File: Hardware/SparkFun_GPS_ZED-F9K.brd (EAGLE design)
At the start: 43.2 x 50.8 mm, 148 parts, among them J3 QWIIC_RIGHT_ANGLE, J4 QWIIC_RIGHT_ANGLE, U1 DUAL-OPTO_HCPL-073L, U2 U-BLOX_ZED_F9R, U3 UHS_INVERTER_SCHMITT_TRIGGERS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, U4 UHS_INVERTER_SCHMITT_TRIGGERS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, U5 3.3V

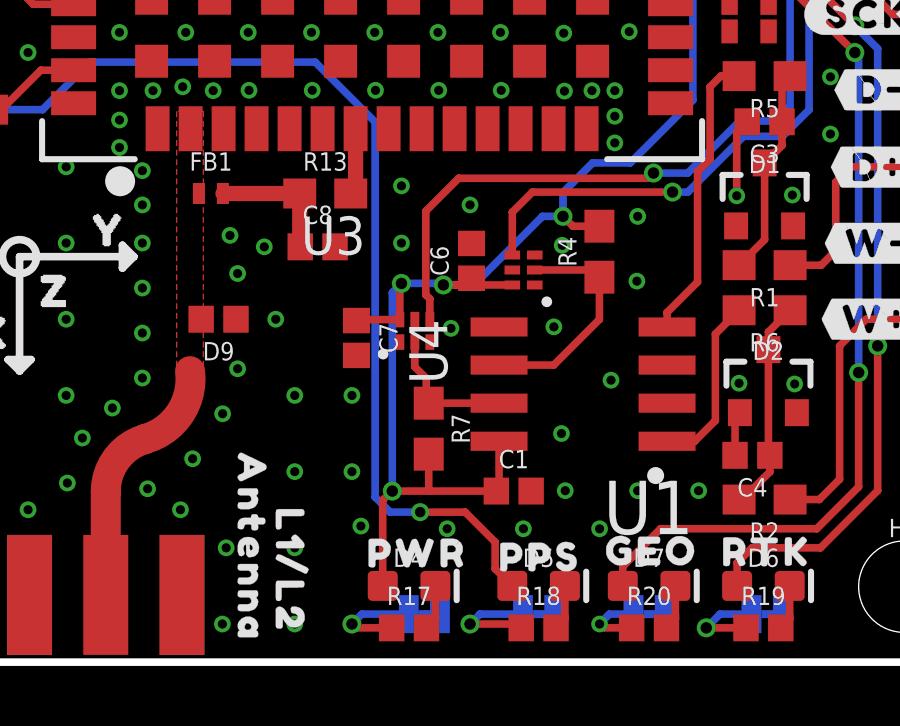
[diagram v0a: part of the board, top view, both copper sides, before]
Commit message: Updates libraries, replaces F9R with F9K, fixes some text in schematic, deletes blank sheets in schematic
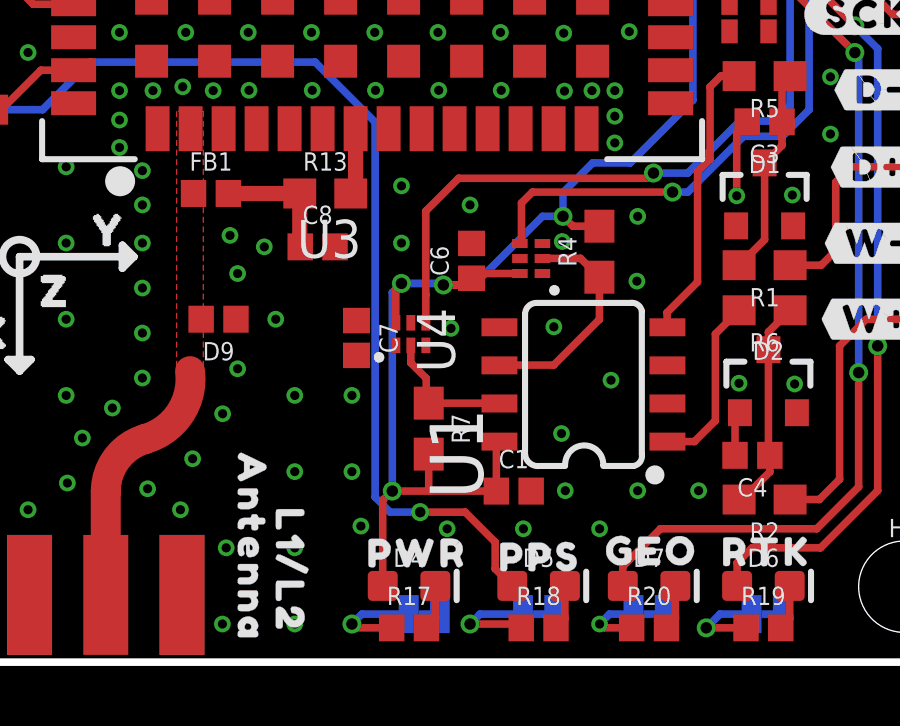
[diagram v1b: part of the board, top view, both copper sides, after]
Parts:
- FB1: value 120NH -> 120Ω; device SparkFun-Coils:0402_MURATA -> SparkFun-Coils:0402
- U1: value DUAL-OPTO_HCPL-073L -> DUAL-OPTO_HCPL-073LSOIC-8; device SparkFun-DiscreteSemi:SOP_8-PIN -> SparkFun-DiscreteSemi:SO08
- U2: value U-BLOX_ZED_F9R -> U-BLOX_ZED_F9K; device SparkFun-GPS:UBLOX_ZED_F9R -> f9k:UBLOX_ZED_F9K
- moved U4 0.46 mm to (28.2, 13.5)
- moved U1 0.19 mm to (29.9, 9.26), turned to 90 degrees
- moved U3 0.17 mm to (24.2, 10.9)
- renumbered JP1 to PWR, JP2 to PPS, JP3 to RTK, JP4 to GEO, JP5 to SPI
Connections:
- net 3.3V: now also U1.8; no longer U1.P8
- net DIR_IN: now also U1.4; no longer U1.P4
- net DIR_SCHMITT: now also U1.6; no longer U1.P6
- net GND: now also U1.2, U1.3, U1.5; no longer U1.P2, U1.P3, U1.P5
- net N$5: now also FB1.2; no longer FB1.P2
- net RF_IN: now also FB1.1; no longer FB1.P1
- net WT_IN: now also U1.1; no longer U1.P1
- net WT_SCHMITT: now also U1.7; no longer U1.P7
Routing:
- net 3.3V: track 133.9 -> 133.4 mm

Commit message: Updates script being used
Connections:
- net DIR_SCHMITT renamed DIR_INV
- net WT_SCHMITT renamed WT_INV
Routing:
- net 3.3V: track 133.4 -> 134.7 mm
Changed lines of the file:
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@@
 <setting verticaltext="up"/>
 </settings>
-<grid distance="0.05" unitdist="inch" unit="inch" style="lines" multiple="1" display="yes" altdistance="0.005" altunitdist="inch" altunit="inch"/>
+<grid distance="0.05" unitdist="inch" unit="inch" style="dots" multiple="1" display="yes" altdistance="0.005" altunitdist="inch" altunit="inch"/>
 <layers>
 <layer number="1" name="Top" color="4" fill="1" visible="yes" active="yes"/>
@@
 <layer number="19" name="Unrouted" color="6" fill="1" visible="yes" active="yes"/>
 <layer number="20" name="Dimension" color="15" fill="1" visible="yes" active="yes"/>
-<layer number="21" name="tPlace" color="16" fill="1" visible="no" active="yes"/>
-<layer number="22" name="bPlace" color="14" fill="1" visible="no" active="yes"/>
+<layer number="21" name="tPlace" color="16" fill="1" visible="yes" active="yes"/>
+<layer number="22" name="bPlace" color="14" fill="1" visible="yes" active="yes"/>
 <layer number="23" name="tOrigins" color="15" fill="1" visible="yes" active="yes"/>
 <layer number="24" name="bOrigins" color="15" fill="1" visible="yes" active="yes"/>
@@
 <layer number="37" name="tTest" color="7" fill="1" visible="no" active="yes"/>
 <layer number="38" name="bTest" color="7" fill="1" visible="no" active="yes"/>
-<layer number="39" name="tKeepout" color="4" fill="11" visible="yes" active="yes"/>
+<layer number="39" name="tKeepout" color="4" fill="11" visible="no" active="yes"/>
 <layer number="40" name="bKeepout" color="1" fill="11" visible="no" active="yes"/>
 <layer number="41" name="tRestrict" color="4" fill="10" visible="no" active="yes"/>
@@
 <layer number="115" name="ReferenceISLANDS" color="7" fill="1" visible="no" active="no"/>
 <layer number="116" name="Patch_BOT" color="9" fill="4" visible="no" active="no"/>
-<layer number="117" name="PM_Ref" color="26" fill="1" visible="no" active="yes"/>
+<layer number="117" name="PM_Ref" color="26" fill="1" visible="yes" active="yes"/>
 <layer number="118" name="Rect_Pads" color="7" fill="1" visible="no" active="no"/>
-<layer number="119" name="PF_Ref" color="31" fill="1" visible="no" active="yes"/>
-<layer number="120" name="WFL_Ref" color="25" fill="1" visible="no" active="yes"/>
+<layer number="119" name="PF_Ref" color="31" fill="1" visible="yes" active="yes"/>
+<layer number="120" name="WFL_Ref" color="25" fill="1" visible="yes" active="yes"/>
 <layer number="121" name="_tsilk" color="7" fill="1" visible="no" active="no"/>
 <layer number="122" name="_bsilk" color="7" fill="1" visible="no" active="no"/>
@@
 <wire x1="26.213" y1="12.796" x2="26.371" y2="12.954" width="0.254" layer="1"/>
 <wire x1="26.371" y1="12.954" x2="27.825" y2="12.954" width="0.254" layer="1"/>
-<wire x1="23.6888" y1="11.31" x2="22.4104" y2="11.418" width="0" layer="19" extent="1-1"/>
+<wire x1="22.3772" y1="11.3848" x2="23.614" y2="11.3848" width="0.254" layer="1"/>
+<wire x1="23.614" y1="11.3848" x2="23.6888" y2="11.31" width="0.254" layer="1"/>
 </signal>
 <signal name="SCL/CLK">
@@
 <wire x1="3.175" y1="18.415" x2="7" y2="18.415" width="0.254" layer="1"/>
 <wire x1="7" y1="18.415" x2="8.5167" y2="18.415" width="0.254" layer="1"/>
-<wire x1="8.7376" y1="18.1941" x2="8.5167" y2="18.415" width="0.254" layer="1"/>
 <wire x1="27.571" y1="2.54" x2="27" y2="3.111" width="0.254" layer="1"/>
 <wire x1="27" y1="3.111" x2="27" y2="4" width="0.254" layer="1"/>
@@
 <wire x1="32.73" y1="11.1738" x2="32.73" y2="11.6546" width="0.254" layer="1"/>
 </signal>
-<signal name="WT_SCHMITT">
+<signal name="WT_INV">
 <contactref element="R7" pad="1"/>
 <contactref element="U1" pad="7"/>
-<wire x1="24.7856" y1="8.632" x2="24.7854" y2="8.6322" width="0.254" layer="1"/>
 <wire x1="24.7854" y1="8.6322" x2="24.7015" y2="8.7161" width="0.254" layer="1"/>
 <wire x1="24.7015" y1="8.7161" x2="24.7015" y2="9.4615" width="0.254" layer="1"/>
@@
 <wire x1="24.7015" y1="9.4615" x2="24.1888" y2="9.9742" width="0.254" layer="1"/>
 </signal>
-<signal name="DIR_SCHMITT">
+<signal name="DIR_INV">
 <contactref element="R4" pad="1"/>
 <contactref element="U1" pad="6"/>

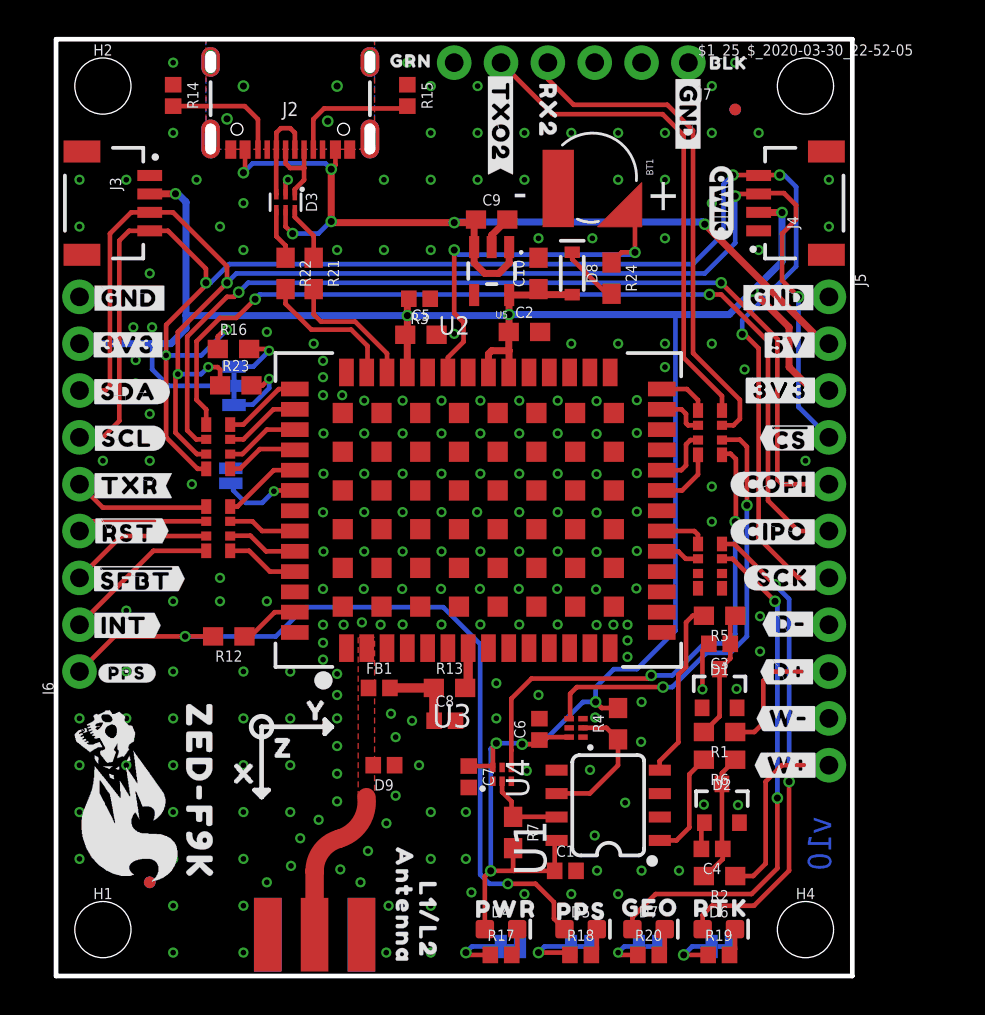
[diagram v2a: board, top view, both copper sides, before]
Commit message: Moves traces for better ground pour and to reduce cross talk
* Replaces all capacitors with smaller footprint
* Replaces 2.2K resistors with 4.7K resistors
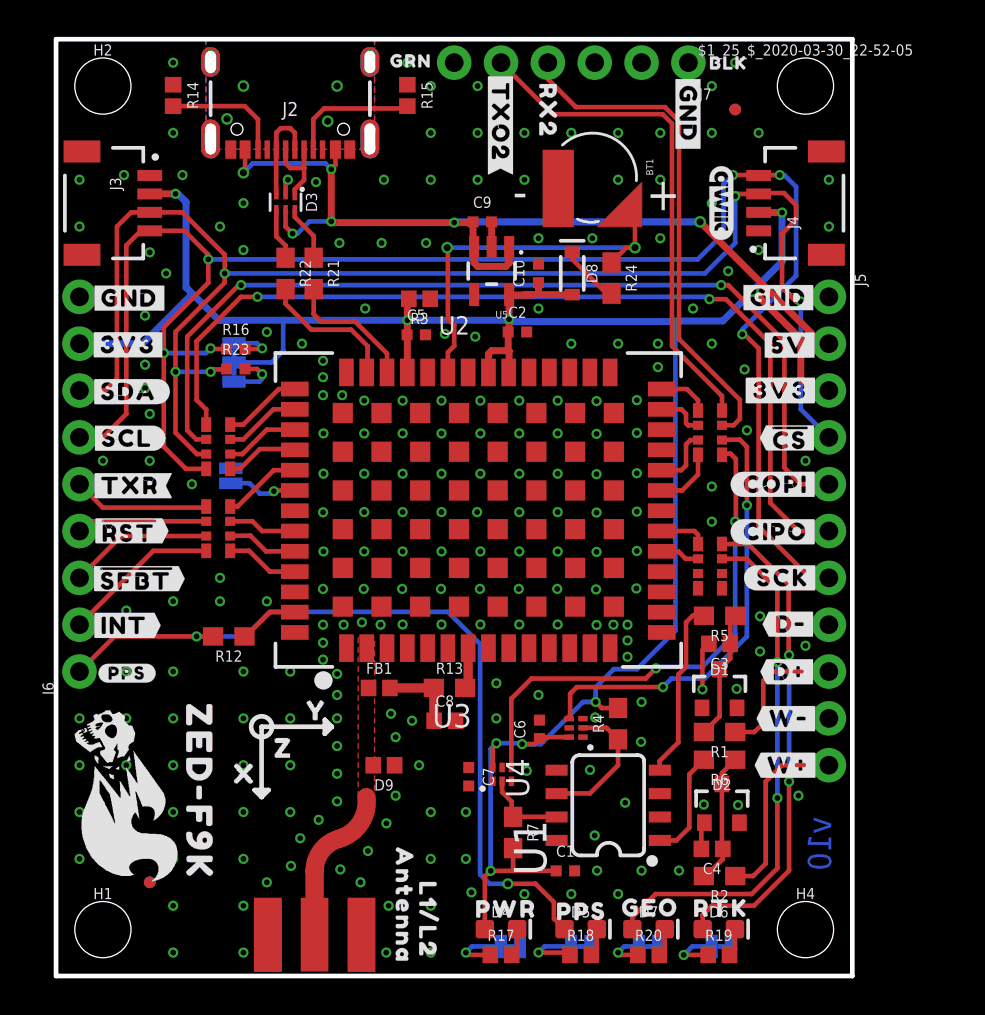
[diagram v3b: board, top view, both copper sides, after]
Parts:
- C1, C6, C7: device SparkFun-Capacitors:0402 -> SparkFun-Capacitors:0402-TIGHT
- C10, C2, C9: device SparkFun-Capacitors:0603 -> SparkFun-Capacitors:0402-TIGHT
- C5: value 1.0uF -> 0.1uF; device SparkFun-Capacitors:0603 -> SparkFun-Capacitors:0402-TIGHT
- R16, R23: value 2.2k -> 4.7k; device SparkFun-Resistors:0603 -> SparkFun-Resistors:0402-TIGHT
- moved JP6 1.27 mm to (9.65, 33.3)
- moved R23 0.89 mm to (9.75, 32.9)
- moved C9 0.52 mm to (23.1, 40.9)
- moved C2 0.38 mm to (25.0, 34.9)
- moved C5 0.25 mm to (19.5, 34.8)
- moved R16 0.13 mm to (9.75, 34.0)
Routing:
- net 3.3V: track 134.7 -> 129.8 mm
- net SCL/CLK: track 97.9 -> 95.9 mm
- net N$1: track 3.90 -> 2.89 mm
- net PPS: track 44.3 -> 43.5 mm
- net N$3: track 3.39 -> 2.58 mm
- net VIN: track 50.7 -> 50.1 mm
- net D_SEL: track 4.34 -> 3.77 mm
- net RXI/COPI: track 51.3 -> 50.8 mm
- net GND: track 6.79 -> 6.31 mm, vias 216 -> 225

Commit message: Adds some leftover adjustments from the last commit
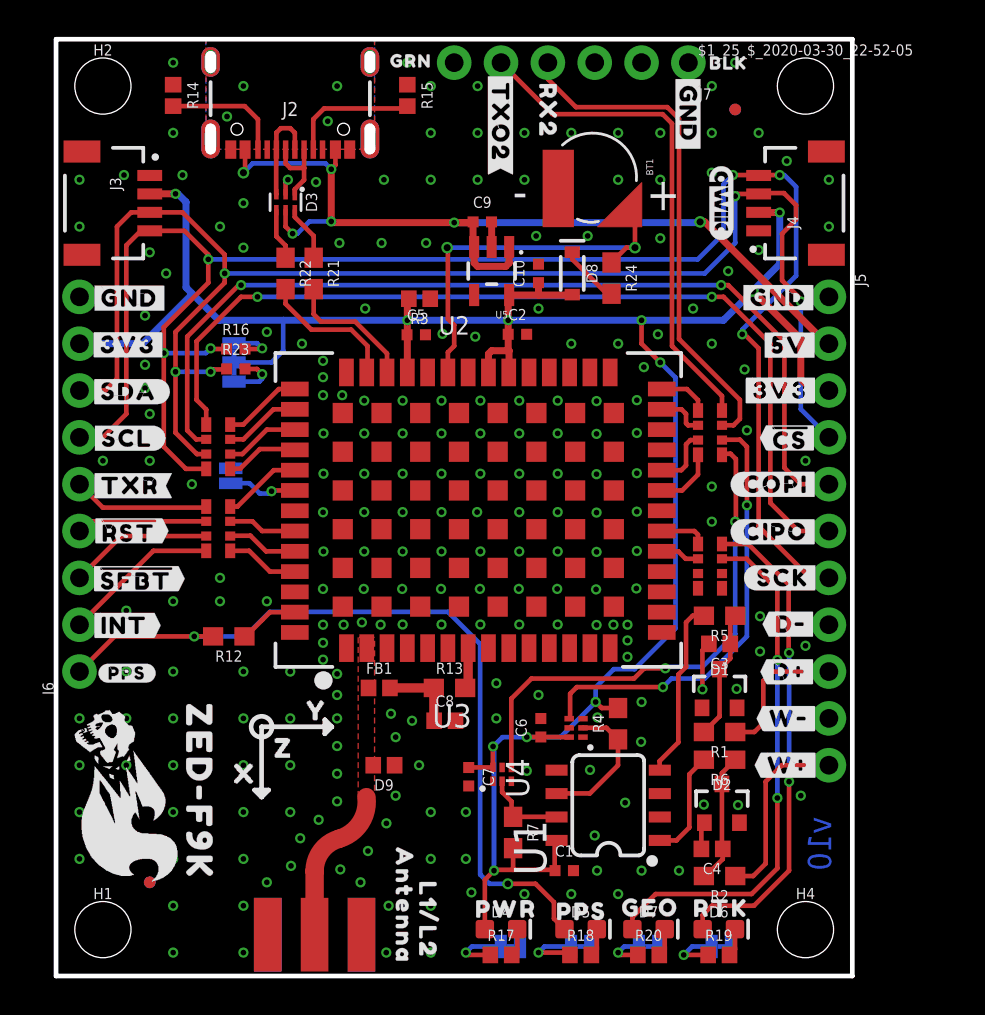
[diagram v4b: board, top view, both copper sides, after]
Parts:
- moved U$54 1.27 mm to (11.3, 33.4)
- moved C2 0.13 mm to (25.0, 34.8)
- moved C6 0.11 mm to (26.3, 13.5)
- moved C1 0.06 mm to (27.6, 5.71)
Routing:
- net 3.3V: track 129.8 -> 131.9 mm, vias 9 -> 11
- net VIN: track 50.1 -> 51.1 mm
- net GND: vias 225 -> 226

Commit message: Flips FTDI header, adds testpoint for VBAT, fixes dimension line width
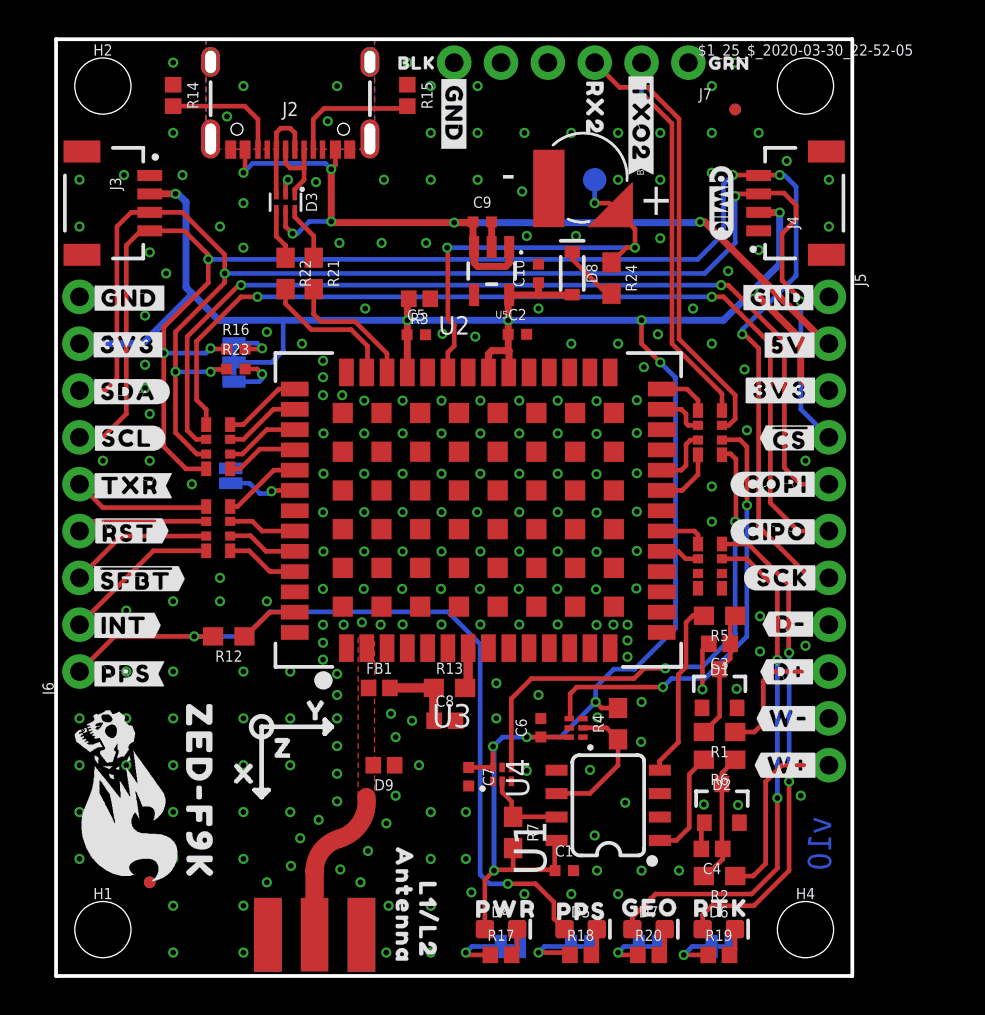
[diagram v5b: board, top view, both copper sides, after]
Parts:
- added TP1: TEST-POINT3X5, SparkFun-Connectors:PAD.03X.05
- U$71: device silk:#PPS#21 -> silk:#PPS#20
- moved U$26 17.3 mm to (36.5, 49.5)
- moved U$64 17.3 mm to (36.5, 49.5)
- moved U$23 16.9 mm to (19.6, 49.5)
- moved U$61 16.9 mm to (19.5, 49.5)
- moved U$17 12.7 mm to (21.6, 46.8)
- moved U$58 12.7 mm to (21.5, 46.8)
- moved U$60 7.62 mm to (31.7, 46.3)
- moved U$18 7.62 mm to (31.7, 46.3)
- moved U$21 2.54 mm to (29.2, 47.0)
- moved U$59 2.54 mm to (29.2, 46.6)
- moved BT1 0.51 mm to (28.6, 43.3)
- moved U$71 0.05 mm to (3.81, 16.4)
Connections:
- net GND: now also J7.6; no longer J7.1
- net RXI2: now also J7.3; no longer J7.4
- net TXO2: now also J7.2; no longer J7.5
- net V_BATT: now also TP1.1
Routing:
- net TXO2: track 27.3 -> 20.8 mm, vias 0 -> 1
- net RXI2: track 27.6 -> 24.2 mm
- net V_BATT: track 20.8 -> 23.9 mm, vias 2 -> 3

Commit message: Changes name of I2C jumper to I2C, it was previously JP6
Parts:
- renumbered JP6 to I2C
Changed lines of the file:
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@@
 <attribute name="VALUE" value="4.7k" x="9.7477" y="34.00104375" size="1.778" layer="27" display="off"/>
 </element>
-<element name="JP6" library="SparkFun-Jumpers" package="SMT-JUMPER_3_2-NC_TRACE_SILK" package3d_urn="urn:adsk.eagle:package:39289/1" value="JUMPER-SMT_3_2-NC_TRACE_SILK" x="9.652" y="33.274" smashed="yes" rot="MR90">
+<element name="I2C" library="SparkFun-Jumpers" package="SMT-JUMPER_3_2-NC_TRACE_SILK" package3d_urn="urn:adsk.eagle:package:39289/1" value="JUMPER-SMT_3_2-NC_TRACE_SILK" x="9.652" y="33.274" smashed="yes" rot="MR90">
 <attribute name="NAME" x="10.795" y="33.274" size="0.6096" layer="26" font="vector" ratio="20" rot="MR90" align="bottom-center"/>
 <attribute name="VALUE" x="8.509" y="33.274" size="0.6096" layer="28" font="vector" ratio="20" rot="MR90" align="top-center"/>
@@
 </signal>
 <signal name="3.3V">
-<contactref element="JP6" pad="2"/>
+<contactref element="I2C" pad="2"/>
 <contactref element="J3" pad="2"/>
 <contactref element="D8" pad="A"/>
@@
 <signal name="N$1">
 <contactref element="R23" pad="2"/>
-<contactref element="JP6" pad="1"/>
+<contactref element="I2C" pad="1"/>
 <via x="11.176" y="32.639" extent="1-16" drill="0.3048"/>
 <wire x1="11.176" y1="32.639" x2="11.176" y2="32.385" width="0.254" layer="16"/>
@@
 </signal>
 <signal name="N$3">
-<contactref element="JP6" pad="3"/>
+<contactref element="I2C" pad="3"/>
 <contactref element="R16" pad="2"/>
 <via x="11.176" y="34.036" extent="1-16" drill="0.3048"/>
